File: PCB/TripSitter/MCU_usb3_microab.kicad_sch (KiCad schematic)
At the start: 9 parts, among them IC4 IP4220CZ6, J8 USB3_B_Micro

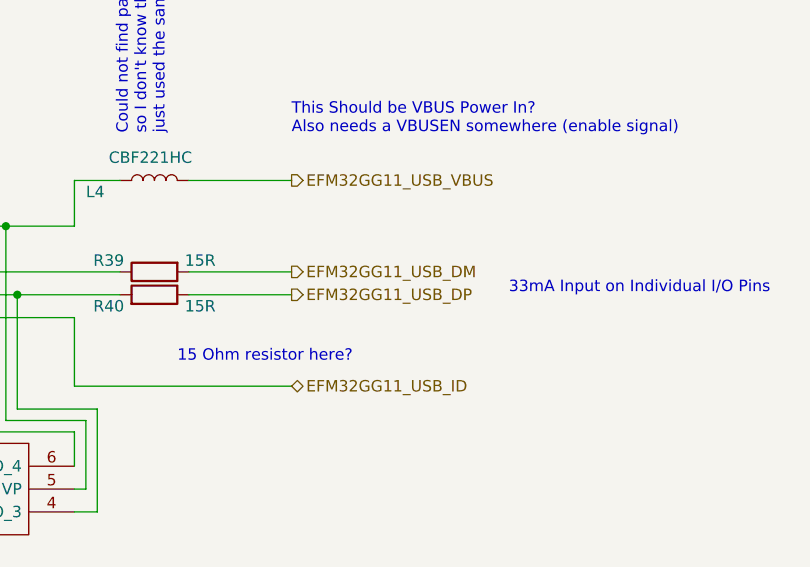
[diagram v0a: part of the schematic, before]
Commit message: change usb footprint to usb3 footprint
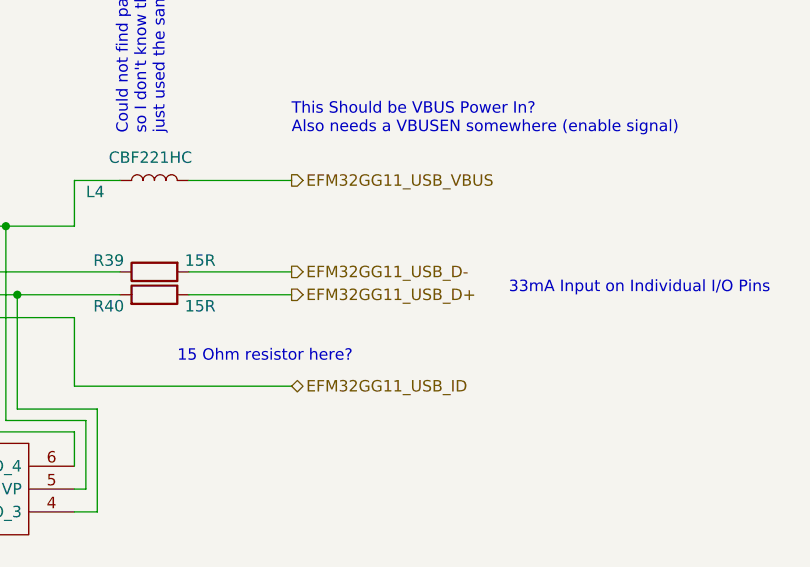
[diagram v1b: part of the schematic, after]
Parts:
- J8: footprint Connector_USB:USB_Micro-B_Wuerth_629105150521_CircularHoles -> footprints:CONN_897-10-010-00-300002_MIM
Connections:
- net EFM32GG11_USB_DM renamed EFM32GG11_USB_D-
- net EFM32GG11_USB_DP renamed EFM32GG11_USB_D+
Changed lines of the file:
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@@
     (effects (font (size 1.27 1.27)) (justify left bottom))
   )
-  (hierarchical_label "EFM32GG11_USB_DM" (shape output) (at 184.15 86.36 0) (fields_autoplaced)
+  (hierarchical_label "EFM32GG11_USB_D-" (shape output) (at 184.15 86.36 0) (fields_autoplaced)
     (effects (font (size 1.27 1.27)) (justify left))
   )
@@
     (effects (font (size 1.27 1.27)) (justify left))
   )
-  (hierarchical_label "EFM32GG11_USB_DP" (shape output) (at 184.15 88.9 0) (fields_autoplaced)
+  (hierarchical_label "EFM32GG11_USB_D+" (shape output) (at 184.15 88.9 0) (fields_autoplaced)
     (effects (font (size 1.27 1.27)) (justify left))
   )
@@
       (effects (font (size 1.27 1.27)))
     )
-    (property "Footprint" "Connector_USB:USB_Micro-B_Wuerth_629105150521_CircularHoles" (at 100.33 87.63 0)
-      (effects (font (size 1.27 1.27)) hide)
-    )
+    (property "Footprint" "footprints:CONN_897-10-010-00-300002_MIM" (at 100.33 87.63 0)
+      (effects (font (size 1.27 1.27)) hide)
+    )
